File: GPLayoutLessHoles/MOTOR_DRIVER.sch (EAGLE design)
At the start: 94 parts, among them T1 2N2222, T2 2N2222, U7 ATMEGA328P_TQFP, Y1 16MHz

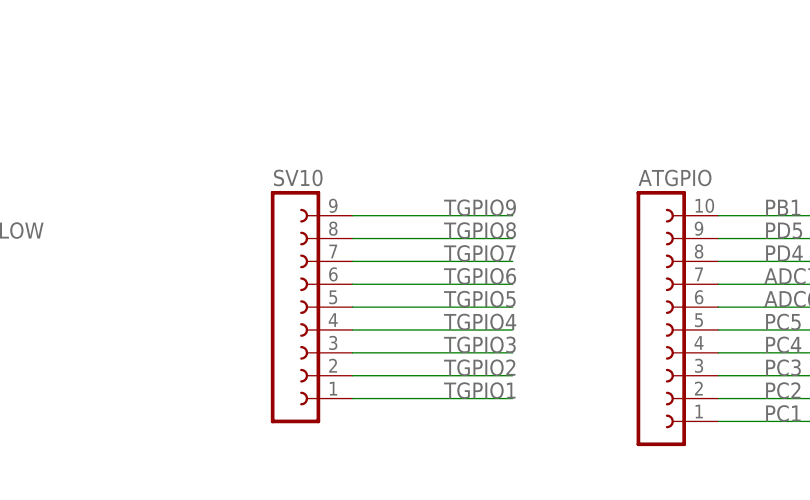
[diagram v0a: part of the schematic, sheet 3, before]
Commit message: reduced GPIOs on teensy and started on atmega
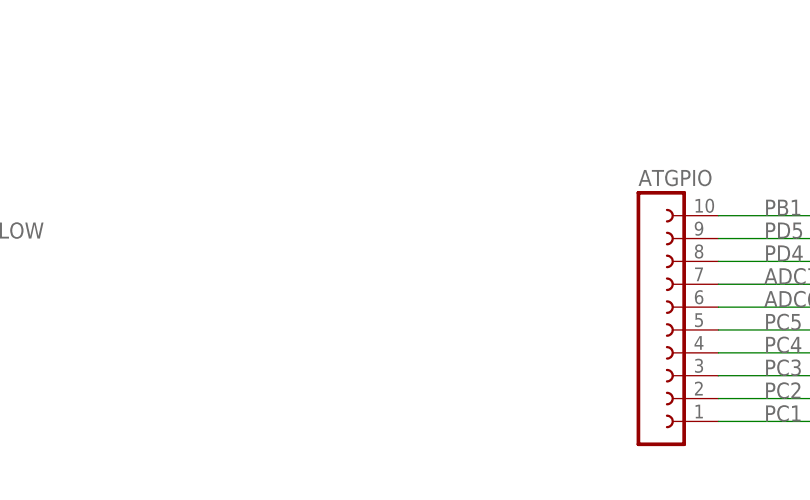
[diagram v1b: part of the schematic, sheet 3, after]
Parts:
- removed SV10: (no value), con-lsta:FE09-1
- U$1: value TEENSY_3.5/3.6_BASIC -> TEENSY_3.5/3.6_FEWER; device Teensy356:TEENSY_3.5/3.6_BASIC -> Teensy356:TEENSY_3.5/3.6_FEWER
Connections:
- removed net TGPIO1: SV10.1, U$1.33/A14
- removed net TGPIO2: SV10.2, U$1.34/A15
- removed net TGPIO3: SV10.3, U$1.35/A16
- removed net TGPIO4: SV10.4, U$1.36/A17
- removed net TGPIO5: SV10.5, U$1.37/A18
- removed net TGPIO6: SV10.6, U$1.38/A19
- removed net TGPIO7: SV10.7, U$1.39/A20
- removed net TGPIO8: SV10.8, U$1.A21/DAC0
- removed net TGPIO9: SV10.9, U$1.A22/DAC1
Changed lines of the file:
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@@
 <part name="MOTOR_NEG" library="solpad" deviceset="SE14" device=""/>
 <part name="FRAME2" library="frames" deviceset="A3L-LOC" device=""/>
-<part name="U$1" library="Teensy356" deviceset="TEENSY_3.5/3.6_BASIC" device="">
+<part name="U$1" library="Teensy356" deviceset="TEENSY_3.5/3.6_FEWER" device="">
 <attribute name="DIGIKEY_PART_NUMBER" value="1568-1443-ND"/>
 <attribute name="MANUFACTURER" value="SparkFun Electronics"/>
@@
 <part name="REC" library="con-lsta" deviceset="FE06-1" device=""/>
 <part name="C8" library="rcl" deviceset="C-US" device="C0805" value="10u"/>
-<part name="SV10" library="con-lsta" deviceset="FE09-1" device=""/>
 <part name="SV6" library="con-lsta" deviceset="FE05-1" device=""/>
 <part name="SV5" library="con-lsta" deviceset="FE08-1" device=""/>
@@
 </segment>
 </net>
-<net name="TGPIO1" class="0">
-<segment>
-<pinref part="U$1" gate="G$1" pin="33/A14"/>
-<wire x1="279.4" y1="109.22" x2="294.64" y2="109.22" width="0.1524" layer="91"/>
-<label x="287.02" y="109.22" size="1.778" layer="95"/>
-</segment>
-</net>
-<net name="TGPIO2" class="0">
-<segment>
-<pinref part="U$1" gate="G$1" pin="34/A15"/>
-<wire x1="279.4" y1="111.76" x2="294.64" y2="111.76" width="0.1524" layer="91"/>
-<label x="287.02" y="111.76" size="1.778" layer="95"/>
-</segment>
-</net>
-<net name="TGPIO3" class="0">
-<segment>
-<pinref part="U$1" gate="G$1" pin="35/A16"/>
-<wire x1="279.4" y1="114.3" x2="294.64" y2="114.3" width="0.1524" layer="91"/>
-<label x="287.02" y="114.3" size="1.778" layer="95"/>
-</segment>
-</net>
-<net name="TGPIO4" class="0">
-<segment>
-<pinref part="U$1" gate="G$1" pin="36/A17"/>
-<wire x1="279.4" y1="116.84" x2="294.64" y2="116.84" width="0.1524" layer="91"/>
-<label x="287.02" y="116.84" size="1.778" layer="95"/>
-</segment>
-</net>
-<net name="TGPIO5" class="0">
-<segment>
-<pinref part="U$1" gate="G$1" pin="37/A18"/>
-<wire x1="279.4" y1="119.38" x2="294.64" y2="119.38" width="0.1524" layer="91"/>
-<label x="287.02" y="119.38" size="1.778" layer="95"/>
-</segment>
-</net>
-<net name="TGPIO6" class="0">
-<segment>
-<pinref part="U$1" gate="G$1" pin="38/A19"/>
-<wire x1="279.4" y1="121.92" x2="294.64" y2="121.92" width="0.1524" layer="91"/>
-<label x="287.02" y="121.92" size="1.778" layer="95"/>
-</segment>
-</net>
-<net name="TGPIO7" class="0">
-<segment>
-<pinref part="U$1" gate="G$1" pin="39/A20"/>
-<wire x1="279.4" y1="124.46" x2="294.64" y2="124.46" width="0.1524" layer="91"/>
-<label x="287.02" y="124.46" size="1.778" layer="95"/>
-</segment>
-</net>
-<net name="TGPIO8" class="0">
-<segment>
-<pinref part="U$1" gate="G$1" pin="A21/DAC0"/>
-<wire x1="279.4" y1="127" x2="294.64" y2="127" width="0.1524" layer="91"/>
-<label x="287.02" y="127" size="1.778" layer="95"/>
-</segment>
-</net>
 <net name="I_SENSE" class="0">
 <segment>
@@
 <wire x1="287.02" y1="71.12" x2="269.24" y2="71.12" width="0.1524" layer="91"/>
 <label x="269.24" y="71.12" size="1.778" layer="95"/>
-</segment>
-</net>
-<net name="TGPIO9" class="0">
-<segment>
-<pinref part="U$1" gate="G$1" pin="A22/DAC1"/>
-<wire x1="279.4" y1="129.54" x2="294.64" y2="129.54" width="0.1524" layer="91"/>
-<label x="287.02" y="129.54" size="1.778" layer="95"/>
 </segment>
 </net>
@@
 <instance part="ATGPIO" gate="G$1" x="162.56" y="66.04"/>
 <instance part="REC" gate="G$1" x="208.28" y="91.44"/>
-<instance part="SV10" gate="G$1" x="121.92" y="68.58"/>
 <instance part="SV6" gate="G$1" x="96.52" y="205.74"/>
 <instance part="SV5" gate="G$1" x="48.26" y="213.36"/>
@@
 </segment>
 </net>
-<net name="TGPIO1" class="0">
-<segment>
-<wire x1="129.54" y1="58.42" x2="147.32" y2="58.42" width="0.1524" layer="91"/>
-<label x="139.7" y="58.42" size="1.778" layer="95"/>
-<pinref part="SV10" gate="G$1" pin="1"/>
-</segment>
-</net>
-<net name="TGPIO2" class="0">
-<segment>
-<wire x1="129.54" y1="60.96" x2="147.32" y2="60.96" width="0.1524" layer="91"/>
-<label x="139.7" y="60.96" size="1.778" layer="95"/>
-<pinref part="SV10" gate="G$1" pin="2"/>
-</segment>
-</net>
-<net name="TGPIO3" class="0">
-<segment>
-<wire x1="129.54" y1="63.5" x2="147.32" y2="63.5" width="0.1524" layer="91"/>
-<label x="139.7" y="63.5" size="1.778" layer="95"/>
-<pinref part="SV10" gate="G$1" pin="3"/>
-</segment>
-</net>
-<net name="TGPIO4" class="0">
-<segment>
-<wire x1="129.54" y1="66.04" x2="147.32" y2="66.04" width="0.1524" layer="91"/>
-<label x="139.7" y="66.04" size="1.778" layer="95"/>
-<pinref part="SV10" gate="G$1" pin="4"/>
-</segment>
-</net>
-<net name="TGPIO5" class="0">
-<segment>
-<wire x1="129.54" y1="68.58" x2="147.32" y2="68.58" width="0.1524" layer="91"/>
-<label x="139.7" y="68.58" size="1.778" layer="95"/>
-<pinref part="SV10" gate="G$1" pin="5"/>
-</segment>
-</net>
-<net name="TGPIO6" class="0">
-<segment>
-<wire x1="129.54" y1="71.12" x2="147.32" y2="71.12" width="0.1524" layer="91"/>
-<label x="139.7" y="71.12" size="1.778" layer="95"/>
-<pinref part="SV10" gate="G$1" pin="6"/>
-</segment>
-</net>
-<net name="TGPIO7" class="0">
-<segment>
-<wire x1="129.54" y1="73.66" x2="147.32" y2="73.66" width="0.1524" layer="91"/>
-<label x="139.7" y="73.66" size="1.778" layer="95"/>
-<pinref part="SV10" gate="G$1" pin="7"/>
-</segment>
-</net>
-<net name="TGPIO8" class="0">
-<segment>
-<wire x1="129.54" y1="76.2" x2="147.32" y2="76.2" width="0.1524" layer="91"/>
-<label x="139.7" y="76.2" size="1.778" layer="95"/>
-<pinref part="SV10" gate="G$1" pin="8"/>
-</segment>
-</net>
 <net name="REC_MOTOR" class="0">
 <segment>
@@
 </segment>
 </net>
-<net name="TGPIO9" class="0">
-<segment>
-<pinref part="SV10" gate="G$1" pin="9"/>
-<wire x1="129.54" y1="78.74" x2="147.32" y2="78.74" width="0.1524" layer="91"/>
-<label x="139.7" y="78.74" size="1.778" layer="95"/>
-</segment>
-</net>

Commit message: more edits
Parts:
- SV2: device con-lsta:FE10-1 -> con-lsta:FE05-1
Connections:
- net MOTOR_HIGH: now also SV2.4; no longer SV2.5
- net MOTOR_LOW: now also SV2.5; no longer SV2.6
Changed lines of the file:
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@@
 <part name="D4" library="diode" deviceset="BYV32" device=""/>
 <part name="SV1" library="con-lsta" deviceset="FE10-1" device=""/>
-<part name="SV2" library="con-lsta" deviceset="FE10-1" device=""/>
+<part name="SV2" library="con-lsta" deviceset="FE05-1" device=""/>
 <part name="FRAME4" library="frames" deviceset="A3L-LOC" device=""/>
 <part name="BATT_HIGH" library="solpad" deviceset="SE14" device=""/>
@@
 <instance part="SUPPLY8" gate="GND" x="45.72" y="53.34"/>
 <instance part="SV1" gate="G$1" x="48.26" y="144.78"/>
-<instance part="SV2" gate="G$1" x="96.52" y="144.78"/>
+<instance part="SV2" gate="G$1" x="101.6" y="139.7"/>
 <instance part="CAMERA" gate="G$1" x="208.28" y="116.84">
 <attribute name="MANUFACTURER" x="208.28" y="116.84" size="1.778" layer="96" display="off"/>
@@
 <net name="MOTOR_HIGH" class="0">
 <segment>
-<pinref part="SV2" gate="G$1" pin="5"/>
-<wire x1="104.14" y1="144.78" x2="127" y2="144.78" width="0.1524" layer="91"/>
-<label x="124.46" y="144.78" size="1.778" layer="95"/>
+<pinref part="SV2" gate="G$1" pin="4"/>
+<wire x1="109.22" y1="142.24" x2="127" y2="142.24" width="0.1524" layer="91"/>
+<label x="124.46" y="142.24" size="1.778" layer="95"/>
 </segment>
 </net>
 <net name="MOTOR_LOW" class="0">
-<segment>
-<pinref part="SV2" gate="G$1" pin="6"/>
-<wire x1="104.14" y1="147.32" x2="127" y2="147.32" width="0.1524" layer="91"/>
-<label x="124.46" y="147.32" size="1.778" layer="95"/>
-</segment>
 <segment>
 <pinref part="S1" gate="G$1" pin="8"/>
 <wire x1="58.42" y1="76.2" x2="45.72" y2="76.2" width="0.1524" layer="91"/>
 <label x="45.72" y="76.2" size="1.778" layer="95"/>
+</segment>
+<segment>
+<pinref part="SV2" gate="G$1" pin="5"/>
+<wire x1="109.22" y1="144.78" x2="127" y2="144.78" width="0.1524" layer="91"/>
+<label x="124.46" y="144.78" size="1.778" layer="95"/>
 </segment>
 </net>
@@
 <segment>
 <pinref part="SV2" gate="G$1" pin="2"/>
-<wire x1="104.14" y1="137.16" x2="127" y2="137.16" width="0.1524" layer="91"/>
+<wire x1="109.22" y1="137.16" x2="127" y2="137.16" width="0.1524" layer="91"/>
 <label x="124.46" y="137.16" size="1.778" layer="95"/>
 </segment>
@@
 <segment>
 <pinref part="SV2" gate="G$1" pin="1"/>
-<wire x1="104.14" y1="134.62" x2="127" y2="134.62" width="0.1524" layer="91"/>
+<wire x1="109.22" y1="134.62" x2="127" y2="134.62" width="0.1524" layer="91"/>
 <label x="124.46" y="134.62" size="1.778" layer="95"/>
 </segment>
@@
 <segment>
 <pinref part="SV2" gate="G$1" pin="3"/>
-<wire x1="104.14" y1="139.7" x2="127" y2="139.7" width="0.1524" layer="91"/>
+<wire x1="109.22" y1="139.7" x2="127" y2="139.7" width="0.1524" layer="91"/>
 <label x="124.46" y="139.7" size="1.778" layer="95"/>
 </segment>

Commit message: more edits
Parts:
- 3_3V, 5V: device con-lsta:FE05-1 -> con-lstb:MA03-1
- GROUND: device con-lsta:FE05-1 -> con-lsta:FE04-1
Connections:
- net 3_3V: no longer 3_3V.4, 3_3V.5
- net 5V: no longer 5V.4, 5V.5
- net GND: no longer GROUND.5
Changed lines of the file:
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@@
 <part name="LED2_CONN" library="con-lsta" deviceset="FE02-1" device=""/>
 <part name="SV9" library="con-lsta" deviceset="FE02-1" device=""/>
-<part name="GROUND" library="con-lsta" deviceset="FE05-1" device=""/>
-<part name="3_3V" library="con-lsta" deviceset="FE05-1" device=""/>
-<part name="5V" library="con-lsta" deviceset="FE05-1" device=""/>
+<part name="GROUND" library="con-lsta" deviceset="FE04-1" device=""/>
+<part name="3_3V" library="con-lstb" deviceset="MA03-1" device=""/>
+<part name="5V" library="con-lstb" deviceset="MA03-1" device=""/>
 <part name="R9" library="rcl" deviceset="R-US_" device="R0805" value="59"/>
 <part name="R10" library="rcl" deviceset="R-US_" device="R0805" value="59"/>
@@
 <instance part="SV9" gate="G$1" x="322.58" y="226.06"/>
 <instance part="GROUND" gate="G$1" x="320.04" y="162.56"/>
-<instance part="3_3V" gate="G$1" x="337.82" y="162.56"/>
-<instance part="5V" gate="G$1" x="360.68" y="162.56"/>
+<instance part="3_3V" gate="G$1" x="337.82" y="160.02"/>
+<instance part="5V" gate="G$1" x="360.68" y="160.02"/>
 <instance part="TXRX" gate="G$1" x="210.82" y="76.2"/>
 <instance part="R12" gate="G$1" x="312.42" y="104.14" rot="R90"/>
@@
 </segment>
 <segment>
-<pinref part="GROUND" gate="G$1" pin="5"/>
 <pinref part="GROUND" gate="G$1" pin="4"/>
-<wire x1="327.66" y1="167.64" x2="327.66" y2="165.1" width="0.1524" layer="91"/>
 <pinref part="GROUND" gate="G$1" pin="3"/>
 <wire x1="327.66" y1="165.1" x2="327.66" y2="162.56" width="0.1524" layer="91"/>
-<junction x="327.66" y="165.1"/>
 <pinref part="GROUND" gate="G$1" pin="2"/>
 <wire x1="327.66" y1="162.56" x2="327.66" y2="160.02" width="0.1524" layer="91"/>
@@
 <wire x1="327.66" y1="160.02" x2="327.66" y2="157.48" width="0.1524" layer="91"/>
 <junction x="327.66" y="160.02"/>
-<wire x1="327.66" y1="167.64" x2="332.74" y2="167.64" width="0.1524" layer="91"/>
-<junction x="327.66" y="167.64"/>
-<label x="330.2" y="167.64" size="1.778" layer="95"/>
+<wire x1="327.66" y1="165.1" x2="332.74" y2="165.1" width="0.1524" layer="91"/>
+<junction x="327.66" y="165.1"/>
 </segment>
 <segment>
@@
 </segment>
 <segment>
-<pinref part="5V" gate="G$1" pin="5"/>
-<pinref part="5V" gate="G$1" pin="4"/>
-<wire x1="368.3" y1="167.64" x2="368.3" y2="165.1" width="0.1524" layer="91"/>
 <pinref part="5V" gate="G$1" pin="3"/>
-<wire x1="368.3" y1="165.1" x2="368.3" y2="162.56" width="0.1524" layer="91"/>
-<junction x="368.3" y="165.1"/>
 <pinref part="5V" gate="G$1" pin="2"/>
 <wire x1="368.3" y1="162.56" x2="368.3" y2="160.02" width="0.1524" layer="91"/>
-<junction x="368.3" y="162.56"/>
 <pinref part="5V" gate="G$1" pin="1"/>
 <wire x1="368.3" y1="160.02" x2="368.3" y2="157.48" width="0.1524" layer="91"/>
 <junction x="368.3" y="160.02"/>
-<wire x1="368.3" y1="167.64" x2="375.92" y2="167.64" width="0.1524" layer="91"/>
-<junction x="368.3" y="167.64"/>
 <label x="373.38" y="167.64" size="1.778" layer="95"/>
+<wire x1="368.3" y1="162.56" x2="375.92" y2="162.56" width="0.1524" layer="91"/>
+<junction x="368.3" y="162.56"/>
 </segment>
 </net>
@@
 </segment>
 <segment>
-<pinref part="3_3V" gate="G$1" pin="5"/>
-<pinref part="3_3V" gate="G$1" pin="4"/>
-<wire x1="345.44" y1="167.64" x2="345.44" y2="165.1" width="0.1524" layer="91"/>
 <pinref part="3_3V" gate="G$1" pin="3"/>
-<wire x1="345.44" y1="165.1" x2="345.44" y2="162.56" width="0.1524" layer="91"/>
-<junction x="345.44" y="165.1"/>
 <pinref part="3_3V" gate="G$1" pin="2"/>
 <wire x1="345.44" y1="162.56" x2="345.44" y2="160.02" width="0.1524" layer="91"/>
-<junction x="345.44" y="162.56"/>
 <pinref part="3_3V" gate="G$1" pin="1"/>
 <wire x1="345.44" y1="160.02" x2="345.44" y2="157.48" width="0.1524" layer="91"/>
 <junction x="345.44" y="160.02"/>
-<wire x1="345.44" y1="167.64" x2="350.52" y2="167.64" width="0.1524" layer="91"/>
-<junction x="345.44" y="167.64"/>
 <label x="347.98" y="167.64" size="1.778" layer="95"/>
-</segment>
-</net>
+<wire x1="345.44" y1="162.56" x2="353.06" y2="162.56" width="0.1524" layer="91"/>
+<junction x="345.44" y="162.56"/>
+</segment>
+</net>

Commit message: more edits
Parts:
- C5, C6: device resistor:C-US025-024X044 -> rcl:C-USC0603
- CAMERA_B: device con-lsta:FE05-1 -> con-lstb:MA03-1
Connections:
- net 3_3V: no longer CAMERA_B.2
- net CAMERA_A0_B: now also CAMERA_B.1; no longer CAMERA_B.3
- net CAMERA_CL_B: now also CAMERA_B.2; no longer CAMERA_B.4
- net CAMERA_SI_B: now also CAMERA_B.3; no longer CAMERA_B.5
- net GND: no longer CAMERA_B.1
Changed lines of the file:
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@@
 <attribute name="PRICE" value="$0.36"/>
 </part>
-<part name="C5" library="resistor" deviceset="C-US" device="025-024X044" value="18 pF"/>
-<part name="C6" library="resistor" deviceset="C-US" device="025-024X044" value="18 pF"/>
+<part name="C5" library="rcl" deviceset="C-US" device="C0603" value="18 pF"/>
+<part name="C6" library="rcl" deviceset="C-US" device="C0603" value="18 pF"/>
 <part name="SUPPLY4" library="supply2" deviceset="GND" device=""/>
 <part name="SUPPLY5" library="supply2" deviceset="GND" device=""/>
@@
 <attribute name="PRICE" value="$49.99"/>
 </part>
-<part name="CAMERA_B" library="con-lsta" deviceset="FE05-1" device="">
+<part name="CAMERA_B" library="con-lstb" deviceset="MA03-1" device="">
 <attribute name="DIGIKEY_PART_NUMBER" value="28317-ND"/>
 <attribute name="MANUFACTURER" value="Parallax"/>
@@
 <attribute name="PRICE" x="208.28" y="116.84" size="1.778" layer="96" display="off"/>
 </instance>
-<instance part="CAMERA_B" gate="G$1" x="243.84" y="119.38">
-<attribute name="MANUFACTURER" x="243.84" y="119.38" size="1.778" layer="96" display="off"/>
-<attribute name="DIGIKEY_PART_NUMBER" x="243.84" y="119.38" size="1.778" layer="96" display="off"/>
-<attribute name="MANUFACTURER_PART_NUMBER" x="243.84" y="119.38" size="1.778" layer="96" display="off"/>
-<attribute name="PRICE" x="243.84" y="119.38" size="1.778" layer="96" display="off"/>
+<instance part="CAMERA_B" gate="G$1" x="246.38" y="116.84">
+<attribute name="MANUFACTURER" x="246.38" y="116.84" size="1.778" layer="96" display="off"/>
+<attribute name="DIGIKEY_PART_NUMBER" x="246.38" y="116.84" size="1.778" layer="96" display="off"/>
+<attribute name="MANUFACTURER_PART_NUMBER" x="246.38" y="116.84" size="1.778" layer="96" display="off"/>
+<attribute name="PRICE" x="246.38" y="116.84" size="1.778" layer="96" display="off"/>
 </instance>
 <instance part="BLUETOOTH" gate="G$1" x="243.84" y="93.98">
@@
 </segment>
 <segment>
-<pinref part="CAMERA_B" gate="G$1" pin="1"/>
-<wire x1="251.46" y1="114.3" x2="271.78" y2="114.3" width="0.1524" layer="91"/>
-<label x="254" y="114.3" size="1.778" layer="95"/>
-</segment>
-<segment>
 <pinref part="BLUETOOTH" gate="G$1" pin="3"/>
 <wire x1="251.46" y1="93.98" x2="271.78" y2="93.98" width="0.1524" layer="91"/>
@@
 </segment>
 <segment>
-<pinref part="CAMERA_B" gate="G$1" pin="2"/>
-<wire x1="251.46" y1="116.84" x2="271.78" y2="116.84" width="0.1524" layer="91"/>
-<label x="254" y="116.84" size="1.778" layer="95"/>
-</segment>
-<segment>
 <pinref part="BLUETOOTH" gate="G$1" pin="4"/>
 <wire x1="251.46" y1="96.52" x2="271.78" y2="96.52" width="0.1524" layer="91"/>
@@
 <net name="CAMERA_SI_B" class="0">
 <segment>
-<pinref part="CAMERA_B" gate="G$1" pin="5"/>
-<wire x1="251.46" y1="124.46" x2="271.78" y2="124.46" width="0.1524" layer="91"/>
-<label x="254" y="124.46" size="1.778" layer="95"/>
+<pinref part="CAMERA_B" gate="G$1" pin="3"/>
+<wire x1="254" y1="119.38" x2="271.78" y2="119.38" width="0.1524" layer="91"/>
+<label x="254" y="119.38" size="1.778" layer="95"/>
 </segment>
 </net>
 <net name="CAMERA_CL_B" class="0">
 <segment>
-<pinref part="CAMERA_B" gate="G$1" pin="4"/>
-<wire x1="251.46" y1="121.92" x2="271.78" y2="121.92" width="0.1524" layer="91"/>
-<label x="254" y="121.92" size="1.778" layer="95"/>
+<pinref part="CAMERA_B" gate="G$1" pin="2"/>
+<wire x1="254" y1="116.84" x2="271.78" y2="116.84" width="0.1524" layer="91"/>
+<label x="254" y="116.84" size="1.778" layer="95"/>
 </segment>
 </net>
 <net name="CAMERA_A0_B" class="0">
 <segment>
-<pinref part="CAMERA_B" gate="G$1" pin="3"/>
-<wire x1="251.46" y1="119.38" x2="271.78" y2="119.38" width="0.1524" layer="91"/>
-<label x="254" y="119.38" size="1.778" layer="95"/>
-</segment>
-</net>
+<pinref part="CAMERA_B" gate="G$1" pin="1"/>
+<wire x1="254" y1="114.3" x2="271.78" y2="114.3" width="0.1524" layer="91"/>
+<label x="254" y="114.3" size="1.778" layer="95"/>
+</segment>
+</net>
